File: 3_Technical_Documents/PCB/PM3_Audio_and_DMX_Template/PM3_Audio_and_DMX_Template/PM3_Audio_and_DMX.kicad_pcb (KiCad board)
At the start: 4 copper layers, 66 x 121.9 mm, 103 parts, among them J1 DMX-out, J2 LINE_IN, J3 LINE_OUT, P1 Conn_02x32_Odd_Even, P2 Conn_02x32_Odd_Even, SW1 SW_DPDT_x2, U1 6N136S, U11 OPA2134, U12 OPA2134, U13 TPA6110A2DGN, U2 CRE1S0505SC, U3 ST485E, U4 OPA322, U6 TLV61070ADBV, U7 LT3045xMSE, U8 LD3985M33R_SOT23, U9 CS4271

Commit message: new push
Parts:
- removed the R65 at (62.4, 132.7)
- removed the R8 at (44.0, 81.9)
- removed SW1: SW_DPDT_x2, Button_Switch_SMD:SW_DPDT_CK_JS202011JCQN
- removed U11: OPA2134, Package_SO:SOIC-8_3.9x4.9mm_P1.27mm
- added C10: 10u CER (rec. Murata GJ8), Capacitor_SMD:C_1210_3225Metric, F.Cu at (265.0, 71.9)
- added C26: 4.7u TANTAL, Capacitor_Tantalum_SMD:CP_EIA-3216-18_Kemet-A, F.Cu at (272.4, 77.6)
- added C27: 100n, Capacitor_SMD:C_0603_1608Metric, F.Cu at (269.9, 83.0)
- added C28: 4.7u CER, Capacitor_SMD:C_1210_3225Metric, F.Cu at (265.0, 83.9)
- added C29: 10u CER (rec. Murata GJ8), Capacitor_SMD:C_1210_3225Metric, F.Cu at (265.0, 88.2)
- added C3: 10u, Capacitor_SMD:C_1210_3225Metric, F.Cu at (250.4, 120.4)
- added C32: 100n, Capacitor_SMD:C_0603_1608Metric, F.Cu at (383.5, 85.0)
- added C33: 1u, Capacitor_SMD:C_0805_2012Metric, F.Cu at (386.0, 91.0)
- added C34: 47u, Capacitor_SMD:CP_Elec_6.3x7.7, F.Cu at (340.0, 87.5)
- added C35: 100n, Capacitor_SMD:C_0603_1608Metric, F.Cu at (245.6, 101.3)
- added C36: 1u, Capacitor_SMD:C_0805_2012Metric, F.Cu at (241.3, 97.0)
- added C37: 100n, Capacitor_SMD:C_0603_1608Metric, F.Cu at (245.6, 103.8)
- added C38: 1u, Capacitor_SMD:C_0805_2012Metric, F.Cu at (241.3, 100.0)
- added C39: 100n, Capacitor_SMD:C_0603_1608Metric, F.Cu at (249.6, 93.7)
- added C4: 10u, Capacitor_SMD:C_1210_3225Metric, F.Cu at (250.4, 124.7)
- added C40: 100n, Capacitor_SMD:C_0603_1608Metric, F.Cu at (249.6, 96.2)
- added C43: 1u, Capacitor_SMD:C_0805_2012Metric, F.Cu at (241.3, 106.0)
- added C44: 47u, Capacitor_SMD:CP_Elec_6.3x7.7, F.Cu at (233.9, 104.7)
- added C45: 10n COG/X7R, Capacitor_SMD:C_0603_1608Metric, F.Cu at (246.2, 61.0)
- added C46: 10n COG/X7R, Capacitor_SMD:C_0603_1608Metric, F.Cu at (246.2, 63.5)
- added C47: 10n COG/X7R, Capacitor_SMD:C_0603_1608Metric, F.Cu at (246.2, 66.0)
- added C49: 1u ELEC, Capacitor_SMD:CP_Elec_4x5.8, F.Cu at (340.0, 72.0)
- added C5: 100n, Capacitor_SMD:C_0603_1608Metric, F.Cu at (245.6, 119.5)
- added C50: 1u ELEC, Capacitor_SMD:CP_Elec_4x5.8, F.Cu at (232.5, 68.5)
- added C51: 1u ELEC, Capacitor_SMD:CP_Elec_4x5.8, F.Cu at (232.5, 74.4)
- added C53: 10u, Capacitor_SMD:CP_Elec_4x5.8, F.Cu at (232.5, 86.1)
- added C54: 10u, Capacitor_SMD:CP_Elec_4x5.8, F.Cu at (240.3, 62.7)
- added C55: 10u, Capacitor_SMD:CP_Elec_4x5.8, F.Cu at (240.3, 68.5)
- added C56: 10u, Capacitor_SMD:CP_Elec_4x5.8, F.Cu at (240.3, 74.4)
- added C57: 10n COG/X7R, Capacitor_SMD:C_0603_1608Metric, F.Cu at (246.2, 68.5)
- added C58: 10n COG/X7R, Capacitor_SMD:C_0603_1608Metric, F.Cu at (246.2, 71.0)
- added C59: 470p COG/X7R, Capacitor_SMD:C_0603_1608Metric, F.Cu at (246.2, 73.5)
- added C6: 100n, Capacitor_SMD:C_0603_1608Metric, F.Cu at (245.6, 122.0)
- added C60: 470p COG/X7R, Capacitor_SMD:C_0603_1608Metric, F.Cu at (246.2, 76.1)
- added C62: 470p COG/X7R, Capacitor_SMD:C_0603_1608Metric, F.Cu at (250.2, 63.5)
- added C63: 2n7 COG/X7R, Capacitor_SMD:C_0603_1608Metric, F.Cu at (250.2, 66.0)
- added C64: 2n7 COG/X7R, Capacitor_SMD:C_0603_1608Metric, F.Cu at (250.2, 68.5)
- added C65: 22u, Capacitor_SMD:CP_Elec_6.3x7.7, F.Cu at (362.0, 121.7)
- added C66: 2n2 COG, Capacitor_SMD:C_0603_1608Metric, F.Cu at (18.0, 220.7)
- added C67: 2n2 COG, Capacitor_SMD:C_0603_1608Metric, F.Cu at (16.0, 243.2)
- added C68: 6n8 COG, Capacitor_SMD:C_0603_1608Metric, F.Cu at (15.0, 222.8)
- added C69: 6n8 COG, Capacitor_SMD:C_0603_1608Metric, F.Cu at (4.50, 239.2)
- added C7: 4.7u TANTAL, Capacitor_Tantalum_SMD:CP_EIA-3216-18_Kemet-A, F.Cu at (272.4, 61.3)
- added C70: 2.2nF COG, Capacitor_SMD:C_0603_1608Metric, F.Cu at (382.7, 103.0)
- added C71: 22u, Capacitor_SMD:CP_Elec_6.3x7.7, F.Cu at (12.5, 216.8)
- added C72: 22u, Capacitor_SMD:CP_Elec_6.3x7.7, F.Cu at (7.00, 245.2)
- added C73: 1n5 COG, Capacitor_SMD:C_0603_1608Metric, F.Cu at (10.0, 222.8)
- added C74: 1n5 COG, Capacitor_SMD:C_0603_1608Metric, F.Cu at (9.72, 239.2)
- added C75: 10n COG/X7R, Capacitor_SMD:C_0603_1608Metric, F.Cu at (17.5, 233.8)
- added C76: 470p COG, Capacitor_SMD:C_0603_1608Metric, F.Cu at (18.0, 223.7)
- added C77: 470p COG, Capacitor_SMD:C_0603_1608Metric, F.Cu at (15.3, 237.8)
- added C78: 1u ELEC, Capacitor_SMD:CP_Elec_4x5.8, F.Cu at (7.00, 230.6)
- added C79: 22u, Capacitor_SMD:CP_Elec_6.3x7.7, F.Cu at (24.5, 232.6)
- added C8: 100n, Capacitor_SMD:C_0603_1608Metric, F.Cu at (269.9, 66.8)
- added C80: 22u, Capacitor_SMD:CP_Elec_6.3x7.7, F.Cu at (24.5, 241.6)
- added C9: 4.7u CER, Capacitor_SMD:C_1210_3225Metric, F.Cu at (265.0, 67.6)
- added J4: LINE_OUT, Connector_Audio:Jack_3.5mm_CUI_SJ-3523-SMT_Horizontal, F.Cu at (104.0, 55.0)
- added R2: 0R, Resistor_SMD:R_0603_1608Metric, F.Cu at (245.6, 124.5)
- added R27: 33k2, Resistor_SMD:R_0603_1608Metric, F.Cu at (269.9, 85.5)
- added R28: 200k, Resistor_SMD:R_0603_1608Metric, F.Cu at (269.9, 88.1)
- added R29: 10k, Resistor_SMD:R_0603_1608Metric, F.Cu at (345.0, 105.9)
- added R3: 10k, Resistor_SMD:R_0603_1608Metric, F.Cu at (245.6, 127.1)
- added R30: 10k, Resistor_SMD:R_0603_1608Metric, F.Cu at (349.5, 94.5)
- added R31: 10k, Resistor_SMD:R_0603_1608Metric, F.Cu at (350.0, 61.0)
- added R32: 10k, Resistor_SMD:R_0603_1608Metric, F.Cu at (363.0, 56.5)
- added R34: 10k, Resistor_SMD:R_0603_1608Metric, F.Cu at (254.2, 61.0)
- added R35: 10k, Resistor_SMD:R_0603_1608Metric, F.Cu at (254.2, 63.5)
- added R36: 10k, Resistor_SMD:R_0603_1608Metric, F.Cu at (254.2, 66.0)
- added R37: 634R, Resistor_SMD:R_0603_1608Metric, F.Cu at (254.2, 68.5)
- added R38: 634R, Resistor_SMD:R_0603_1608Metric, F.Cu at (254.2, 71.0)
- added R39: 634R, Resistor_SMD:R_0603_1608Metric, F.Cu at (254.2, 73.5)
- added R4: 10k, Resistor_SMD:R_0603_1608Metric, F.Cu at (245.6, 129.6)
- added R40: 634R, Resistor_SMD:R_0603_1608Metric, F.Cu at (254.2, 76.1)
- added R41: 91R, Resistor_SMD:R_0603_1608Metric, F.Cu at (258.2, 61.0)
- added R42: 91R, Resistor_SMD:R_0603_1608Metric, F.Cu at (258.2, 63.5)
- added R43: 91R, Resistor_SMD:R_0603_1608Metric, F.Cu at (258.2, 66.0)
- added R44: 91R, Resistor_SMD:R_0603_1608Metric, F.Cu at (258.2, 68.5)
- added R45: 4.99k, Resistor_SMD:R_0603_1608Metric, F.Cu at (342.5, 117.0)
- added R46: 4k42, Resistor_SMD:R_0603_1608Metric, F.Cu at (19.5, 220.7)
- added R47: 1k33, Resistor_SMD:R_0603_1608Metric, F.Cu at (15.0, 224.3)
- added R48: 4k42, Resistor_SMD:R_0603_1608Metric, F.Cu at (14.5, 243.2)
- added R49: 1k33, Resistor_SMD:R_0603_1608Metric, F.Cu at (4.50, 237.8)
- added R5: 10k, Resistor_SMD:R_0603_1608Metric, F.Cu at (245.6, 132.1)
- added R50: 1k5, Resistor_SMD:R_0603_1608Metric, F.Cu at (12.5, 223.8)
- added R51: 1k5, Resistor_SMD:R_0603_1608Metric, F.Cu at (7.00, 238.6)
- added R52: 2k32, Resistor_SMD:R_0603_1608Metric, F.Cu at (21.0, 223.7)
- added R53: 715R, Resistor_SMD:R_0603_1608Metric, F.Cu at (10.0, 224.3)
- added R54: 2k32, Resistor_SMD:R_0603_1608Metric, F.Cu at (14.5, 240.2)
- added R55: 715R, Resistor_SMD:R_0603_1608Metric, F.Cu at (9.72, 237.8)
- added R56: 4.99k, Resistor_SMD:R_0603_1608Metric, F.Cu at (19.5, 223.7)
- added R57: 4.99k, Resistor_SMD:R_0603_1608Metric, F.Cu at (16.0, 240.2)
- added R58: 560R, Resistor_SMD:R_0603_1608Metric, F.Cu at (31.0, 232.6)
- added R59: 560R, Resistor_SMD:R_0603_1608Metric, F.Cu at (31.0, 241.6)
- added R6: 33k2, Resistor_SMD:R_0603_1608Metric, F.Cu at (269.9, 69.3)
- added R60: 47k, Resistor_SMD:R_0603_1608Metric, F.Cu at (31.0, 234.1)
- added R61: 47k, Resistor_SMD:R_0603_1608Metric, F.Cu at (31.0, 243.1)
- added R7: 200k, Resistor_SMD:R_0603_1608Metric, F.Cu at (269.9, 71.8)
- added RV2: 50k stereo, Potentiometer_THT:Potentiometer_Bourns_PTV112-4_Dual_Vertical, F.Cu at (256.7, 97.9)
- added RV4: 50k stereo, Potentiometer_THT:Potentiometer_Bourns_PTV112-4_Dual_Vertical, F.Cu at (358.0, 99.3)
- added SW2: SW_DPDT_x2, Button_Switch_SMD:SW_DPDT_CK_JS202011JCQN, F.Cu at (248.9, 136.1)
- added SW3: SW_DPDT_x2, Button_Switch_SMD:SW_DPDT_CK_JS202011JCQN, F.Cu at (261.4, 137.9)
- added U1: ESP32-MINI-1, PCM_Espressif:ESP32-MINI-1, F.Cu at (120.1, 139.0)
- added U10: CS4271, Package_SO:TSSOP-28_4.4x9.7mm_P0.65mm, F.Cu at (247.9, 110.7)
- added U13: OPA2134, Package_SO:SOIC-8_3.9x4.9mm_P1.27mm, F.Cu at (248.4, 87.2)
- added U14: OPA2134, Package_SO:SOIC-8_3.9x4.9mm_P1.27mm, F.Cu at (13.5, 232.1)
- added U2: LT3045xMSE, Package_SO:MSOP-12-1EP_3x4.039mm_P0.65mm_EP1.651x2.845mm, F.Cu at (265.9, 62.7)
- C30: value 100n -> 40p
- C31: value 1u -> 40p; footprint Capacitor_SMD:C_0805_2012Metric -> Capacitor_SMD:C_0603_1608Metric
- C41: value 47u -> 100n; footprint Capacitor_SMD:CP_Elec_6.3x7.7 -> Capacitor_SMD:C_0603_1608Metric
- C42: value 1u ELEC -> 1u; footprint Capacitor_SMD:CP_Elec_4x5.8 -> Capacitor_SMD:C_0805_2012Metric
- C52: value 2.2nF COG -> 1u ELEC; footprint Capacitor_SMD:C_0603_1608Metric -> Capacitor_SMD:CP_Elec_4x5.8
- C61: value 22u -> 470p COG/X7R; footprint Capacitor_SMD:CP_Elec_6.3x7.7 -> Capacitor_SMD:C_0603_1608Metric
- J3: value LINE_OUT -> HEADPHONE_JACK
- RV1: value 50k -> 50k stereo; footprint Potentiometer_THT:Potentiometer_Bourns_PTV09A-1_Single_Vertical -> Potentiometer_THT:Potentiometer_Bourns_PTV112-4_Dual_Vertical
- RV3: value 50k stereo -> 50k; footprint Potentiometer_THT:Potentiometer_Bourns_PTV112-4_Dual_Vertical -> Potentiometer_THT:Potentiometer_Bourns_PTV09A-1_Single_Vertical
- U9: value CS4271 -> LT3045xMSE; footprint Package_SO:TSSOP-28_4.4x9.7mm_P0.65mm -> Package_SO:MSOP-12-1EP_3x4.039mm_P0.65mm_EP1.651x2.845mm
- moved RV3 326.9 mm to (352.4, 74.5), turned to 0 degrees
- moved C48 252.2 mm to (378.0, 63.9)
- moved U12 229.9 mm to (248.4, 80.7), turned to 0 degrees
- moved C41 225.8 mm to (249.6, 98.8)
- moved RV1 223.2 mm to (258.5, 123.7), turned to 0 degrees
- moved C42 221.5 mm to (241.3, 103.0), turned to 0 degrees
- moved U9 220.9 mm to (265.9, 79.0), turned to 0 degrees
- moved C61 219.1 mm to (250.2, 61.0)
- moved Y1 205.9 mm to (232.3, 111.4)
- moved C30 202.0 mm to (245.6, 93.7), turned to 0 degrees
- moved R33 196.1 mm to (250.2, 76.1), turned to 0 degrees
- moved C52 191.4 mm to (232.5, 80.2), turned to 0 degrees
- moved C31 183.4 mm to (245.6, 96.2), turned to 0 degrees
- moved J3 82.2 mm to (133.7, 142.4)
- moved J2 66.2 mm to (104.0, 43.5)
- renumbered C3 to C11, C4 to C12, C5 to C13, C6 to C14, C7 to C15, C8 to C16, C9 to C17, C10 to C18, C18 to C19, C19 to C20, C20 to C21, C21 to C22, C22 to C23, C23 to C24, C24 to C25, C63 to C81, C64 to C82, C65 to C83, C66 to C84, C67 to C85, C68 to C86, C69 to C87, C70 to C88, C71 to C89, R4 to R10, R5 to R11, R6 to R12, R7 to R13, R10 to R14, R11 to R15, R12 to R16, R13 to R17, R14 to R18, R15 to R19, R16 to R20, R25 to R21, R26 to R22, R27 to R23, R28 to R24, R29 to R25, R30 to R26, R70 to R62, R71 to R63, R72 to R64, R73 to R65, R74 to R66, R2 to R8, R3 to R9, TP14 to TP10, TP8 to TP6, TP9 to TP7, TP12 to TP8, TP13 to TP9, U13 to U15, U1 to U3, U2 to U4, U3 to U5, U4 to U6, U6 to U7, U7 to U8
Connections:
- C17 pad 2: +5VA -> VA
- C25 pad 1: +5VA -> VA
- C30 pad 1: unconnected-(C30-Pad1) -> GND
- C30 pad 2: unconnected-(C30-Pad2) -> XTI
- C31 pad 1: unconnected-(C31-Pad1) -> GND
- C31 pad 2: unconnected-(C31-Pad2) -> XTO
- C41 pad 1: unconnected-(C41-Pad1) -> GND
- C41 pad 2: unconnected-(C41-Pad2) -> Net-(U10-FILT+)
- C42 pad 1: unconnected-(C42-Pad1) -> VA
- C42 pad 2: unconnected-(C42-Pad2) -> GND
- C52 pad 1: unconnected-(C52-Pad1) -> VA
- C52 pad 2: unconnected-(C52-Pad2) -> GND
- C61 pad 1: unconnected-(C61-Pad1) -> Net-(C61-Pad1)
- C61 pad 2: unconnected-(C61-Pad2) -> Net-(U13A--)
- C86 pad 1: +5VA -> VA
- C89 pad 1: +5VA -> VA
- J2 pad R: unconnected-(J2-PadR) -> Jack_R
- J2 pad S: unconnected-(J2-PadS) -> GND
- J2 pad T: unconnected-(J2-PadT) -> Jack_L
- J3 pad R: unconnected-(J3-PadR) -> /PM3 Audio/Headphone Amplifier/out_r
- J3 pad S: unconnected-(J3-PadS) -> GND
- J3 pad T: unconnected-(J3-PadT) -> /PM3 Audio/Headphone Amplifier/out_l
- R15 pad 2: +5VA -> VA
- R16 pad 2: +5VA -> VA
- R25 pad 1: +5VA -> VA
- R33 pad 1: unconnected-(R33-Pad1) -> VCOM
- R33 pad 2: unconnected-(R33-Pad2) -> Net-(U12A-+)
- RV1 pad 1: unconnected-(RV1-Pad1) -> GND
- RV1 pad 2: unconnected-(RV1-Pad2) -> /PM3 Audio/Codec with analog line buffers/LINE_IN_R
- RV1 pad 3: unconnected-(RV1-Pad3) -> MIC_JACKR
- TP8 pad 1: +5VA -> VA
- U12 pad 1: unconnected-(U12-Pad1) -> Net-(C59-Pad1)
- U12 pad 2: unconnected-(U12A---Pad2) -> Net-(U12A--)
- U12 pad 3: unconnected-(U12A-+-Pad3) -> Net-(U12A-+)
- U12 pad 4: unconnected-(U12C-V--Pad4) -> GND
- U12 pad 5: unconnected-(U12B-+-Pad5) -> Net-(U12B-+)
- U12 pad 6: unconnected-(U12B---Pad6) -> Net-(U12B--)
- U12 pad 7: unconnected-(U12-Pad7) -> Net-(C60-Pad1)
- U12 pad 8: unconnected-(U12C-V+-Pad8) -> VA
- U15 pad 6: +5VA -> VA
- U6 pad 5: +5VA -> VA
- U8 pad 10: +5VA -> VA
- U8 pad 11: +5VA -> VA
- U8 pad 12: +5VA -> VA
- U9 pad 1: unconnected-(U9-XT0-Pad1) -> /PM3 Audio/Digital Power Supply/+5V
- U9 pad 10: unconnected-(U9-VL-Pad10) -> /PM3 Audio/Digital Power Supply/3V3
- U9 pad 11: unconnected-(U9-SCL/CCLK(M0)-Pad11) -> /PM3 Audio/Digital Power Supply/3V3
- U9 pad 12: unconnected-(U9-SDA/CDIN(M1)-Pad12) -> /PM3 Audio/Digital Power Supply/3V3
- U9 pad 13: unconnected-(U9-AD0/~{CS}(I2S/~{LJ})-Pad13) -> GND
- U9 pad 2: unconnected-(U9-XTI-Pad2) -> /PM3 Audio/Digital Power Supply/+5V
- U9 pad 3: unconnected-(U9-MCLK-Pad3) -> /PM3 Audio/Digital Power Supply/+5V
- U9 pad 4: unconnected-(U9-LRCK-Pad4) -> /PM3 Audio/Digital Power Supply/+5V
- U9 pad 5: unconnected-(U9-SCLK-Pad5) -> Net-(U9-PG)
- U9 pad 6: unconnected-(U9-SDOUT(M/~{S})-Pad6) -> GND
- U9 pad 7: unconnected-(U9-SDIN-Pad7) -> /PM3 Audio/Digital Power Supply/+5V
- U9 pad 8: unconnected-(U9-DGND-Pad8) -> Net-(U9-SET)
- U9 pad 9: unconnected-(U9-VD-Pad9) -> GND
- Y1 pad 1: unconnected-(Y1-Pad1) -> XTO
- Y1 pad 2: unconnected-(Y1-Pad2) -> XTI
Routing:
- net VA: track 0.00 -> 32.5 mm, vias 0 -> 2
- net +5VA: track 32.5 -> 0.00 mm, vias 2 -> 0
- added copper zone on B.Cu, net VA
- added copper zone on In2.Cu, net VA
- removed copper zone on B.Cu, net +5VA
- removed copper zone on In2.Cu, net +5VA

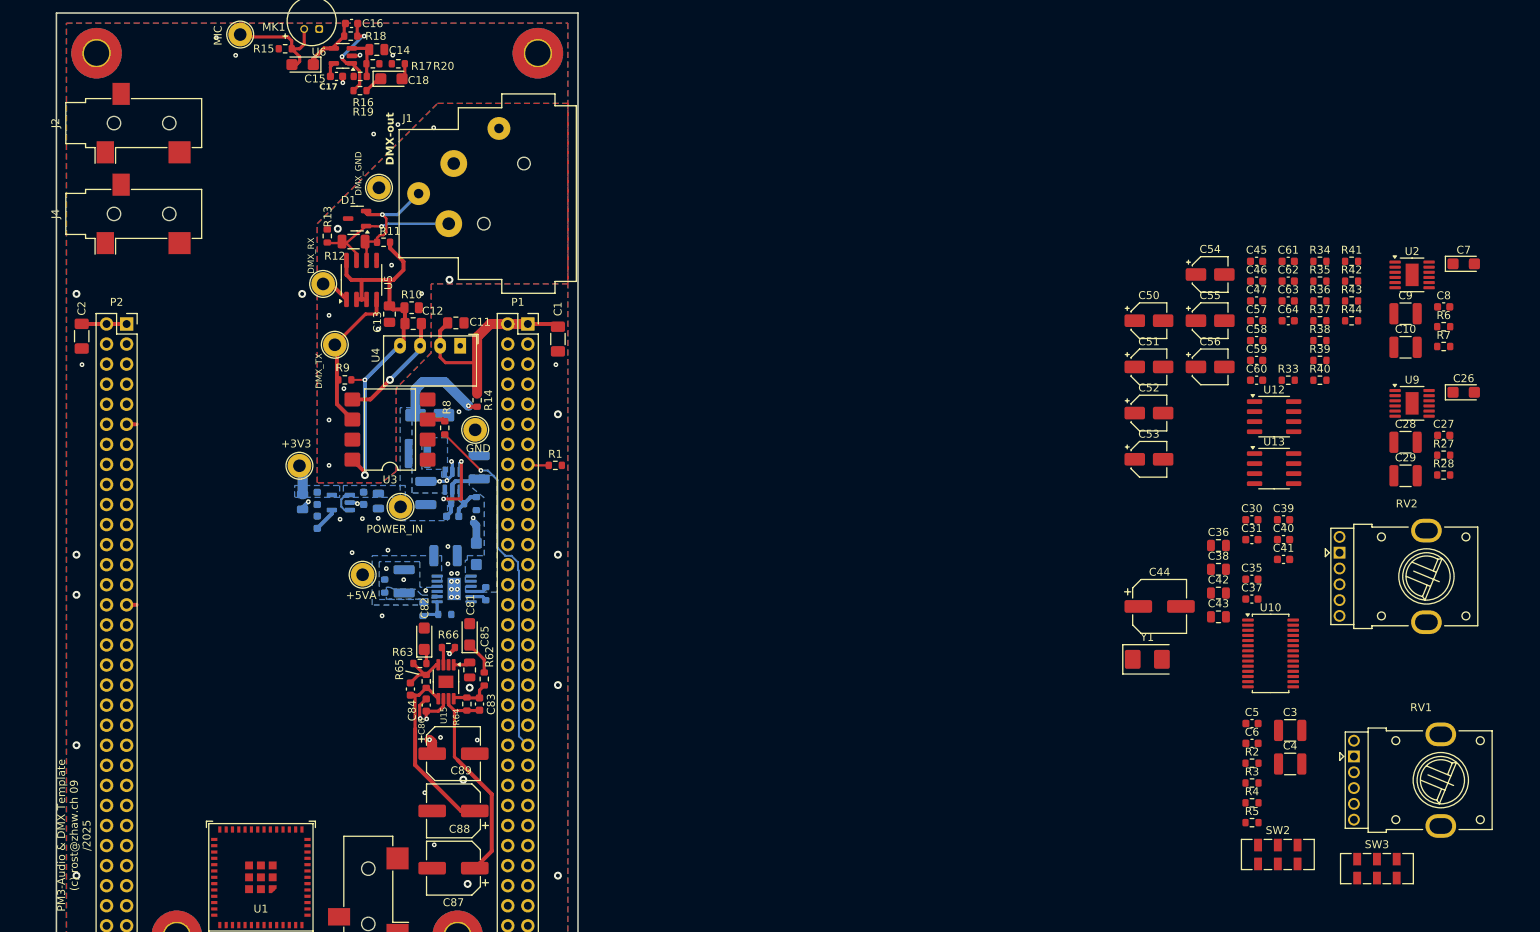
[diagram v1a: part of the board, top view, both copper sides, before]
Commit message: codec and layout
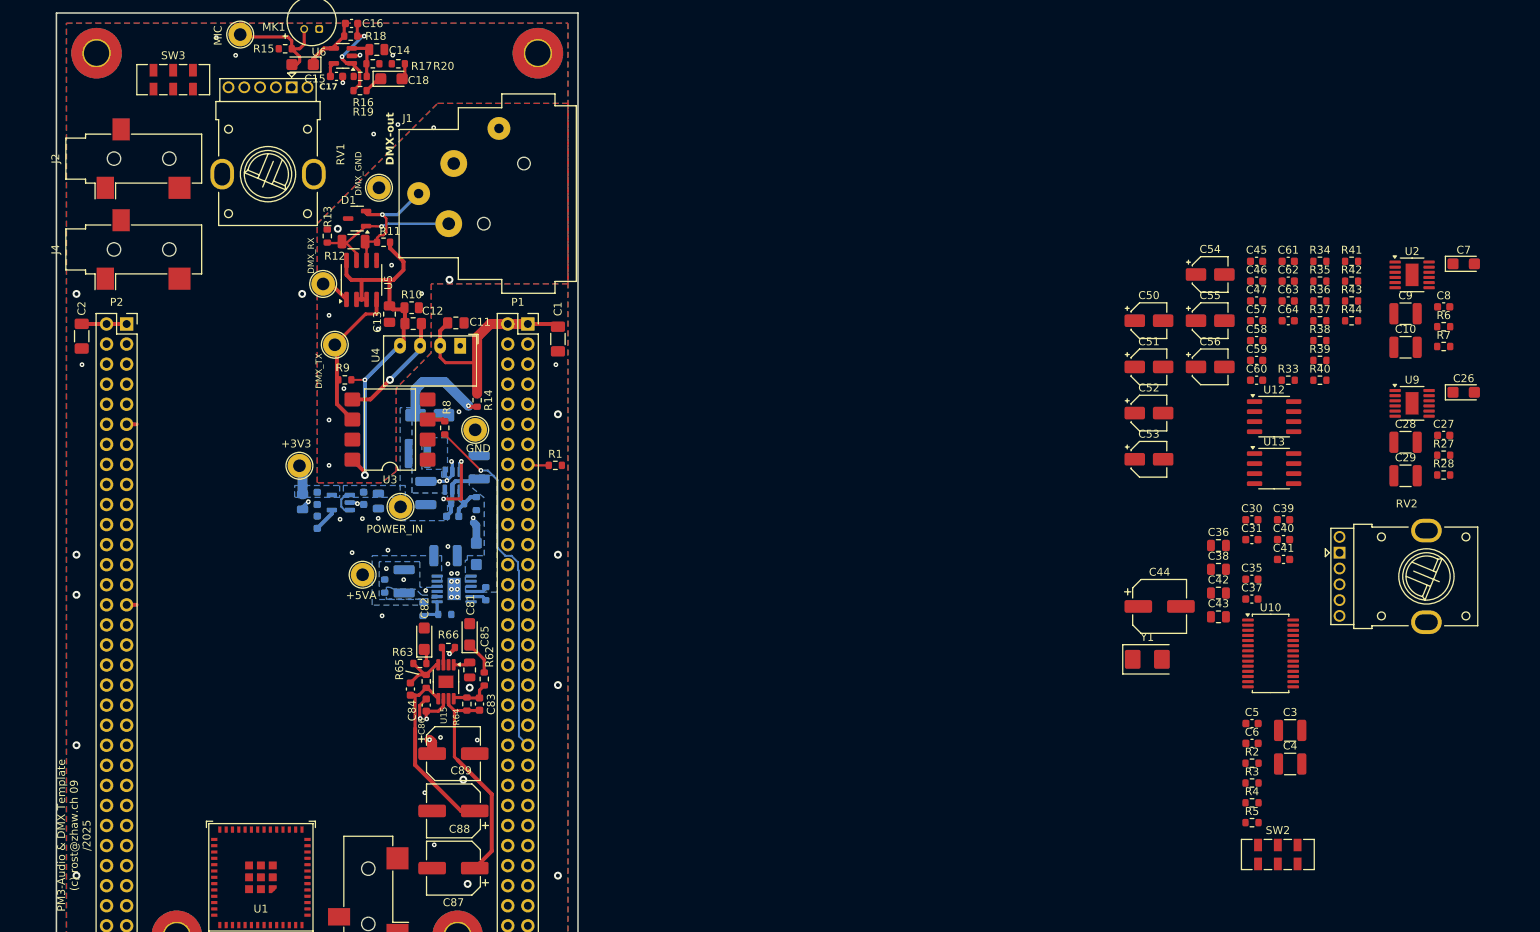
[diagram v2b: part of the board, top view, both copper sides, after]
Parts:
- moved SW3 182.2 mm to (109.0, 38.0)
- moved RV1 159.0 mm to (124.0, 39.0), turned to -90 degrees
- moved J2 4.50 mm to (104.0, 48.0)
- moved J4 4.50 mm to (104.0, 59.5)

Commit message: rework esp32, codec and layout
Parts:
- removed the C66 at (18.0, 220.7)
- removed the C67 at (16.0, 243.2)
- removed the C68 at (15.0, 222.8)
- removed the C69 at (4.50, 239.2)
- removed the C70 at (382.7, 103.0)
- removed the C71 at (12.5, 216.8)
- removed the C72 at (7.00, 245.2)
- removed the C73 at (10.0, 222.8)
- removed the C74 at (9.72, 239.2)
- removed C75: 10n COG/X7R, Capacitor_SMD:C_0603_1608Metric
- removed C76, C77: 470p COG, Capacitor_SMD:C_0603_1608Metric
- removed C78: 1u ELEC, Capacitor_SMD:CP_Elec_4x5.8
- removed C79, C80: 22u, Capacitor_SMD:CP_Elec_6.3x7.7
- removed the R59 at (31.0, 241.6)
- removed the R60 at (31.0, 234.1)
- removed the R61 at (31.0, 243.1)
- removed the R7 at (269.9, 71.8)
- removed RV3: 50k, Potentiometer_THT:Potentiometer_Bourns_PTV09A-1_Single_Vertical
- removed RV4: 50k stereo, Potentiometer_THT:Potentiometer_Bourns_PTV112-4_Dual_Vertical
- removed the SW2 at (248.9, 136.1)
- removed the U14 at (13.5, 232.1)
- added R1: 10k, Resistor_SMD:R_0603_1608Metric, F.Cu at (41.0, 133.0)
- added R26: 33k2, Resistor_SMD:R_0603_1608Metric, F.Cu at (231.4, 77.2)
- added SW2: SW_DPDT_x2, Button_Switch_SMD:SW_DPDT_CK_JS202011JCQN, F.Cu at (211.2, 114.7)
- added SW2: SW_DPDT_x2, Button_Switch_SMD:SW_DPDT_CK_JS202011JCQN, F.Cu at (33.8, 134.5)
- added U11: OPA2134, Package_SO:SOIC-8_3.9x4.9mm_P1.27mm, F.Cu at (168.5, -32.0)
- C34: value 47u -> 100n; footprint Capacitor_SMD:CP_Elec_6.3x7.7 -> Capacitor_SMD:C_0603_1608Metric
- C35, C39, C40: value 100n -> 1u; footprint Capacitor_SMD:C_0603_1608Metric -> Capacitor_SMD:C_0805_2012Metric
- C36, C38: value 1u -> 100n; footprint Capacitor_SMD:C_0805_2012Metric -> Capacitor_SMD:C_0603_1608Metric
- C41: value 100n -> 47u; footprint Capacitor_SMD:C_0603_1608Metric -> Capacitor_SMD:CP_Elec_6.3x7.7
- C42, C43: value 1u -> 10u; footprint Capacitor_SMD:C_0805_2012Metric -> Capacitor_SMD:CP_Elec_4x5.8
- C44: value 47u -> 470p COG/X7R; footprint Capacitor_SMD:CP_Elec_6.3x7.7 -> Capacitor_SMD:C_0603_1608Metric
- C45: value 10n COG/X7R -> 470p COG/X7R
- C46, C47: value 10n COG/X7R -> 2n7 COG/X7R
- C49: value 1u ELEC -> 10n COG/X7R; footprint Capacitor_SMD:CP_Elec_4x5.8 -> Capacitor_SMD:C_0603_1608Metric
- C52: value 1u ELEC -> 2n2 COG; footprint Capacitor_SMD:CP_Elec_4x5.8 -> Capacitor_SMD:C_0603_1608Metric
- C53: value 10u -> 2n2 COG; footprint Capacitor_SMD:CP_Elec_4x5.8 -> Capacitor_SMD:C_0603_1608Metric
- C54, C55: value 10u -> 6n8 COG; footprint Capacitor_SMD:CP_Elec_4x5.8 -> Capacitor_SMD:C_0603_1608Metric
- C56: value 10u -> 22u; footprint Capacitor_SMD:CP_Elec_4x5.8 -> Capacitor_SMD:CP_Elec_6.3x7.7
- C57: value 10n COG/X7R -> 22u; footprint Capacitor_SMD:C_0603_1608Metric -> Capacitor_SMD:CP_Elec_6.3x7.7
- C58: value 10n COG/X7R -> 1n5 COG
- C59: value 470p COG/X7R -> 1n5 COG
- C60: value 470p COG/X7R -> 10n COG/X7R
- C61, C62: value 470p COG/X7R -> 470p COG
- C63: value 2n7 COG/X7R -> 1u ELEC; footprint Capacitor_SMD:C_0603_1608Metric -> Capacitor_SMD:CP_Elec_4x5.8
- C64: value 2n7 COG/X7R -> 22u; footprint Capacitor_SMD:C_0603_1608Metric -> Capacitor_SMD:CP_Elec_6.3x7.7
- R2: value 0R -> 10k
- R27, R6: value 33k2 -> 200k
- R28: value 200k -> 10k
- R32: value 10k -> 47k
- R33, R34, R35, R36: value 10k -> 22R
- R37, R38: value 634R -> 10k
- R43: value 91R -> 4k42
- R44: value 91R -> 1k33
- R45: value 4.99k -> 4k42
- R46: value 4k42 -> 1k33
- R47: value 1k33 -> 1k5
- R48: value 4k42 -> 1k5
- R49: value 1k33 -> 2k32
- R5: value 10k -> 33k2
- R50: value 1k5 -> 715R
- R51: value 1k5 -> 2k32
- R52: value 2k32 -> 715R
- R53: value 715R -> 4.99k
- R54: value 2k32 -> 4.99k
- R55: value 715R -> 560R
- R56: value 4.99k -> 560R
- R57: value 4.99k -> 47k
- R58: value 560R -> 47k
- U1: value ESP32-MINI-1 -> ESP32-WROOM-32E; footprint PCM_Espressif:ESP32-MINI-1 -> RF_Module:ESP32-WROOM-32D; moved to B.Cu
- moved R55 291.5 mm to (100.9, -39.1), turned to 90 degrees
- moved R54 289.6 mm to (119.4, -29.6)
- moved R51 288.0 mm to (119.4, -26.6)
- moved C65 286.8 mm to (122.4, -36.1)
- moved R57 286.3 mm to (100.9, -33.1)
- moved R49 284.0 mm to (106.9, -27.1), turned to -90 degrees
- moved R56 283.9 mm to (126.9, -39.1), turned to 90 degrees
- moved R48 283.2 mm to (122.4, -18.6), turned to 180 degrees
- moved R58 282.5 mm to (126.9, -33.1), turned to 90 degrees
- moved R53 272.3 mm to (106.9, -30.1), turned to 90 degrees
- moved R45 264.0 mm to (120.9, -26.6), turned to 90 degrees
- moved R46 263.3 mm to (122.4, -21.6), turned to 0 degrees
- moved R50 262.0 mm to (104.0, -21.6), turned to 0 degrees
- moved R52 261.3 mm to (122.4, -17.1), turned to 180 degrees
- moved R47 260.2 mm to (104.0, -20.1), turned to 0 degrees
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- renumbered C81 to C66, C82 to C67, C83 to C68, C84 to C69, C85 to C70, C86 to C71, C87 to C72, C88 to C73, C89 to C74, R11 to R10, R12 to R11, R13 to R12, R14 to R13, R15 to R14, R16 to R15, R17 to R16, R18 to R17, R19 to R18, R20 to R19, R21 to R20, R22 to R21, R23 to R22, R24 to R23, R25 to R24, R26 to R25, R62 to R59, R63 to R60, R64 to R61, R65 to R62, R66 to R63, R8 to R7, R9 to R8, R10 to R9, U15 to U14
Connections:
- C2 pad 1: +3V0 -> VL
- C32 pad 1: unconnected-(C32-Pad1) -> VL
- C32 pad 2: unconnected-(C32-Pad2) -> GND
- C33 pad 1: unconnected-(C33-Pad1) -> VL
- C33 pad 2: unconnected-(C33-Pad2) -> GND
- C34 pad 1: unconnected-(C34-Pad1) -> VD
- C34 pad 2: unconnected-(C34-Pad2) -> GND
- C35 pad 1: VA -> VD
- C37 pad 1: VA -> VCOM
- C38 pad 1: VA -> GND
- C38 pad 2: GND -> Net-(U10-FILT+)
- C41 pad 1: GND -> Net-(U10-FILT+)
- C41 pad 2: Net-(U10-FILT+) -> GND
- C42 pad 1: VA -> Net-(U11A-+)
- C42 pad 2: GND -> /PM3 Audio/Codec with analog line buffers/LINE_IN_L
- C43 pad 1: VCOM -> Net-(U11B-+)
- C43 pad 2: GND -> /PM3 Audio/Codec with analog line buffers/LINE_IN_R
- C44 pad 1: Net-(U10-FILT+) -> Net-(C44-Pad1)
- C44 pad 2: GND -> Net-(U11A--)
- C45 pad 1: VA -> Net-(C45-Pad1)
- C45 pad 2: GND -> Net-(U11B--)
- C46 pad 1: VA -> /PM3 Audio/Codec with analog line buffers/Audio Input/AINA
- C46 pad 2: GND -> VCOM
- C47 pad 1: VA -> VCOM
- C47 pad 2: GND -> /PM3 Audio/Codec with analog line buffers/Audio Input/AINB
- C48 pad 1: unconnected-(C48-Pad1) -> VA
- C48 pad 2: unconnected-(C48-Pad2) -> GND
- C49 pad 1: unconnected-(C49-Pad1) -> VA
- C49 pad 2: unconnected-(C49-Pad2) -> GND
- C52 pad 1: VA -> GND
- C52 pad 2: GND -> Net-(C52-Pad2)
- C53 pad 1: Net-(U12A-+) -> GND
- C53 pad 2: /PM3 Audio/Codec with analog line buffers/LINE_IN_L -> Net-(C53-Pad2)
- C54 pad 1: Net-(U12B-+) -> GND
- C54 pad 2: /PM3 Audio/Codec with analog line buffers/LINE_IN_R -> Net-(C54-Pad2)
- C55 pad 1: Net-(U13A-+) -> GND
- C55 pad 2: /PM3 Audio/Codec with analog line buffers/LINE_IN_L -> Net-(C55-Pad2)
- C56 pad 1: Net-(U13B-+) -> Net-(C56-Pad1)
- C56 pad 2: /PM3 Audio/Codec with analog line buffers/LINE_IN_R -> GND
- C57 pad 1: GND -> Net-(C57-Pad1)
- C57 pad 2: VCOM -> GND
- C58 pad 2: VCOM -> Net-(U13A-+)
- C59 pad 1: Net-(C59-Pad1) -> GND
- C59 pad 2: Net-(U12A--) -> Net-(U13B-+)
- C60 pad 1: Net-(C60-Pad1) -> VA
- C60 pad 2: Net-(U12B--) -> GND
- C61 pad 1: Net-(C61-Pad1) -> Net-(U13A--)
- C61 pad 2: Net-(U13A--) -> Net-(C61-Pad2)
- C62 pad 1: Net-(C62-Pad1) -> Net-(U13B--)
- C62 pad 2: Net-(U13B--) -> Net-(C62-Pad2)
- C63 pad 1: /PM3 Audio/Codec with analog line buffers/Audio Input/AINA -> VA
- C63 pad 2: /PM3 Audio/Codec with analog line buffers/Audio Input/VQ2 -> GND
- C64 pad 1: /PM3 Audio/Codec with analog line buffers/Audio Input/AINB -> Net-(C61-Pad2)
- C64 pad 2: /PM3 Audio/Codec with analog line buffers/Audio Input/VQ3 -> Net-(C64-Pad2)
- C65 pad 1: unconnected-(C65-Pad1) -> Net-(C62-Pad2)
- C65 pad 2: unconnected-(C65-Pad2) -> Net-(C65-Pad2)
- P2 pad 1: +3V0 -> VL
- P2 pad 2: +3V0 -> VL
- P2 pad 49: unconnected-(P2-Pin_49-Pad49) -> _PB13
- P2 pad 50: unconnected-(P2-Pin_50-Pad50) -> _PB12
- P2 pad 51: unconnected-(P2-Pin_51-Pad51) -> _PB15
- P2 pad 52: unconnected-(P2-Pin_52-Pad52) -> _PB14
- R2 pad 1: /ESP32/Digital Power Supply/+5V -> EN
- R2 pad 2: +5V -> +3V3_ESP
- R27 pad 1: Net-(U9-SET) -> /PM3 Audio/Digital Power Supply/+5V
- R27 pad 2: GND -> Net-(U9-PG)
- R28 pad 1: /PM3 Audio/Digital Power Supply/+5V -> PA8
- R28 pad 2: Net-(U9-PG) -> VL
- R29 pad 1: unconnected-(R29-Pad1) -> GND
- R29 pad 2: unconnected-(R29-Pad2) -> PA8
- R3 pad 1: EN -> BOOT
- R3 pad 2: +3V3_ESP -> Net-(SW2A-B)
- R30 pad 1: unconnected-(R30-Pad1) -> PC9
- R30 pad 2: unconnected-(R30-Pad2) -> VL
- R31 pad 1: unconnected-(R31-Pad1) -> GND
- R31 pad 2: unconnected-(R31-Pad2) -> PC9
- R32 pad 1: unconnected-(R32-Pad1) -> PE6
- R32 pad 2: unconnected-(R32-Pad2) -> VL
- R33 pad 1: VCOM -> PE2
- R33 pad 2: Net-(U12A-+) -> Net-(U10-MCLK)
- R34 pad 1: Net-(U12B-+) -> Net-(U10-LRCK)
- R34 pad 2: VCOM -> PE4
- R35 pad 1: VCOM -> Net-(U10-SCLK)
- R35 pad 2: Net-(U13A-+) -> PE5
- R36 pad 1: Net-(U13B-+) -> Net-(U10-SDIN)
- R36 pad 2: VCOM -> PE3
- R37 pad 1: Net-(U12A--) -> VCOM
- R37 pad 2: /PM3 Audio/Codec with analog line buffers/Audio Input/AINA -> Net-(U11A-+)
- R38 pad 1: Net-(U12B--) -> Net-(U11B-+)
- R38 pad 2: /PM3 Audio/Codec with analog line buffers/Audio Input/VQ2 -> VCOM
- R39 pad 1: Net-(U13A--) -> Net-(U11A--)
- R39 pad 2: /PM3 Audio/Codec with analog line buffers/Audio Input/AINB -> /PM3 Audio/Codec with analog line buffers/Audio Input/AINA
- R4 pad 1: BOOT1 -> BOOT2
- R40 pad 1: Net-(U13B--) -> Net-(U11B--)
- R40 pad 2: /PM3 Audio/Codec with analog line buffers/Audio Input/VQ3 -> /PM3 Audio/Codec with analog line buffers/Audio Input/AINB
- R41 pad 1: Net-(C59-Pad1) -> Net-(C44-Pad1)
- R42 pad 1: Net-(C60-Pad1) -> Net-(C45-Pad1)
- R42 pad 2: /PM3 Audio/Codec with analog line buffers/Audio Input/VQ2 -> /PM3 Audio/Codec with analog line buffers/Audio Input/AINB
- R43 pad 1: Net-(C61-Pad1) -> /PM3 Audio/Codec with analog line buffers/Audio Output/AOUTA-
- R43 pad 2: /PM3 Audio/Codec with analog line buffers/Audio Input/AINB -> Net-(C52-Pad2)
- R44 pad 1: Net-(C62-Pad1) -> /PM3 Audio/Codec with analog line buffers/Audio Output/AOUTA+
- R44 pad 2: /PM3 Audio/Codec with analog line buffers/Audio Input/VQ3 -> Net-(C54-Pad2)
- R45 pad 1: unconnected-(R45-Pad1) -> /PM3 Audio/Codec with analog line buffers/Audio Output/AOUTB-
- R45 pad 2: unconnected-(R45-Pad2) -> Net-(C53-Pad2)
- R46 pad 1: /PM3 Audio/Codec with analog line buffers/Audio Output/AOUTA- -> /PM3 Audio/Codec with analog line buffers/Audio Output/AOUTB+
- R46 pad 2: Net-(C66-Pad2) -> Net-(C55-Pad2)
- R47 pad 1: /PM3 Audio/Codec with analog line buffers/Audio Output/AOUTA+ -> Net-(C54-Pad2)
- R47 pad 2: Net-(C68-Pad2) -> Net-(C56-Pad1)
- R48 pad 1: /PM3 Audio/Codec with analog line buffers/Audio Output/AOUTB- -> Net-(C55-Pad2)
- R48 pad 2: Net-(C67-Pad2) -> Net-(C57-Pad1)
- R49 pad 1: /PM3 Audio/Codec with analog line buffers/Audio Output/AOUTB+ -> Net-(C52-Pad2)
- R49 pad 2: Net-(C69-Pad2) -> Net-(U13A--)
- R5 pad 1: BOOT2 -> Net-(U2-SET)
- R5 pad 2: Net-(SW2B-B) (its old number) -> GND
- R50 pad 1: Net-(C68-Pad2) -> Net-(C54-Pad2)
- R50 pad 2: Net-(C71-Pad1) -> Net-(U13A-+)
- R51 pad 1: Net-(C69-Pad2) -> Net-(C53-Pad2)
- R51 pad 2: Net-(C72-Pad1) -> Net-(U13B--)
- R52 pad 1: Net-(C66-Pad2) -> Net-(C55-Pad2)
- R52 pad 2: Net-(U14A--) -> Net-(U13B-+)
- R53 pad 1: Net-(C68-Pad2) -> Net-(C52-Pad2)
- R53 pad 2: Net-(U14A-+) -> Net-(C61-Pad2)
- R54 pad 1: Net-(C67-Pad2) -> Net-(C53-Pad2)
- R54 pad 2: Net-(U14B--) -> Net-(C62-Pad2)
- R55 pad 1: Net-(C69-Pad2) -> Net-(C64-Pad2)
- R55 pad 2: Net-(U14B-+) -> /PM3 Audio/Codec with analog line buffers/LINE_OUT_L
- R56 pad 1: Net-(C66-Pad2) -> Net-(C65-Pad2)
- R56 pad 2: Net-(C76-Pad2) -> /PM3 Audio/Codec with analog line buffers/LINE_OUT_R
- R57 pad 1: Net-(C67-Pad2) -> GND
- R57 pad 2: Net-(C77-Pad2) -> /PM3 Audio/Codec with analog line buffers/LINE_OUT_L
- R58 pad 1: Net-(C79-Pad2) -> GND
- R58 pad 2: /PM3 Audio/Codec with analog line buffers/LINE_OUT_L -> /PM3 Audio/Codec with analog line buffers/LINE_OUT_R
- R6 pad 1: Net-(U2-SET) -> /ESP32/Digital Power Supply/+5V
- R6 pad 2: GND -> Net-(U2-PG)
- TP9 pad 1: +3.3V -> VD
- U1 pad 10: unconnected-(U1-VDET_2/GPIO35/ADC1_CH7-Pad10) -> LRCLK
- U1 pad 11: unconnected-(U1-32K_XP/GPIO32/ADC1_CH4-Pad11) -> BCLK
- U1 pad 13: unconnected-(U1-GPIO25/ADC2_CH8/DAC_1-Pad13) -> TMS
- U1 pad 14: unconnected-(U1-GPIO26/ADC2_CH9/DAC_2-Pad14) -> TDI
- U1 pad 15: unconnected-(U1-GPIO27/ADC2_CH7-Pad15) -> GND
- U1 pad 16: unconnected-(U1-MTMS/GPIO14/ADC2_CH6-Pad16) -> TCK
- U1 pad 2: GND -> +3V3_ESP
- U1 pad 20: BOOT2 -> unconnected-(U1-NC-Pad20)
- U1 pad 21: BOOT1 -> unconnected-(U1-NC-Pad21)
- U1 pad 23: unconnected-(U1-NC-Pad23) -> TDO
- U1 pad 25: unconnected-(U1-SD_DATA2/GPIO9-Pad25) -> MCLK
- U1 pad 27: GND -> unconnected-(U1-IO16-Pad27)
- U1 pad 28: unconnected-(U1-NC-Pad28) -> Net-(U1-IO17)
- U1 pad 3: +3V3_ESP -> EN
- U1 pad 34: unconnected-(U1-GPIO21-Pad34) -> Rx
- U1 pad 35: unconnected-(U1-U0RXD/GPIO3-Pad35) -> Tx
- U1 pad 36: unconnected-(U1-U0TXD/GPIO1-Pad36) -> DOUT
- U1 pad 37: unconnected-(U1-NC-Pad37) -> DIN
- U1 pad 8: EN -> unconnected-(U1-IO32-Pad8)
- U10 pad 10: VA -> VL
- U10 pad 13: unconnected-(U10-AD0/~{CS}(I2S/~{LJ})-Pad13) -> GND
- U10 pad 16: /PM3 Audio/Codec with analog line buffers/Audio Input/VQ2 -> VCOM
- U10 pad 19: /PM3 Audio/Codec with analog line buffers/Audio Input/VQ3 -> VCOM
- U10 pad 23: unconnected-(U10-~{AMUTEC}-Pad23) -> VL
- U10 pad 28: unconnected-(U10-~{BMUTEC}-Pad28) -> VL
- U10 pad 3: /PM3 Audio/MCLK -> Net-(U10-MCLK)
- U10 pad 4: PE4 -> Net-(U10-LRCK)
- U10 pad 5: PE5 -> Net-(U10-SCLK)
- U10 pad 7: PE3 -> Net-(U10-SDIN)
- U10 pad 9: VA -> VD
- U12 pad 1: Net-(C59-Pad1) -> VCOM
- U12 pad 2: Net-(U12A--) -> VCOM
- U12 pad 3: Net-(U12A-+) -> VCOM
- U12 pad 5: Net-(U12B-+) -> VCOM
- U12 pad 7: Net-(C60-Pad1) -> Net-(U12B--)
- U13 pad 1: Net-(C61-Pad1) -> Net-(C61-Pad2)
- U13 pad 7: Net-(C62-Pad1) -> Net-(C62-Pad2)
- U3 pad 2: +3V0 -> VL
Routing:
- net GND: track 18.3 -> 69.2 mm, vias 54 -> 79
- net VL: track 0.00 -> 37.3 mm, vias 0 -> 3
- net VCOM: track 0.00 -> 31.0 mm, vias 0 -> 2
- net /PM3 Audio/Codec with analog line buffers/LINE_OUT_L: track 0.00 -> 24.9 mm
- net Net-(U13B-+): track 0.00 -> 24.7 mm
- net /PM3 Audio/Codec with analog line buffers/LINE_OUT_R: track 0.00 -> 21.9 mm
- net /PM3 Audio/Codec with analog line buffers/Audio Output/AOUTB-: track 0.00 -> 21.5 mm
- net /PM3 Audio/Codec with analog line buffers/Audio Output/AOUTA-: track 0.00 -> 20.2 mm
- net /PM3 Audio/Codec with analog line buffers/Audio Output/AOUTB+: track 0.00 -> 19.3 mm
- net /ESP32/Digital Power Supply/+5V: track 0.00 -> 18.6 mm
- net Net-(U13A-+): track 0.00 -> 15.8 mm
- net VA: track 32.5 -> 48.2 mm
- net Net-(U13B--): track 0.00 -> 14.3 mm, vias 0 -> 2
- net Net-(C62-Pad2): track 0.00 -> 10.1 mm
- net Net-(U11A-+): track 0.00 -> 9.65 mm
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- added copper zone on B.Cu, net VD
- removed copper zone on B.Cu, net +3.3V
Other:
- board text added: "Analog Input"
- board text added: "Analog Output"
- board text added: "Codec"

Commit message: more layout
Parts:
- moved C30 216.3 mm to (207.2, -27.5)
- moved C31 216.3 mm to (210.2, -27.5)
- moved C37 216.3 mm to (213.2, -15.0)
- moved C38 216.3 mm to (216.8, -21.0)
- moved C40 216.3 mm to (213.2, -13.0)
- moved C41 216.3 mm to (223.4, -25.5)
- moved R28 216.3 mm to (204.3, -16.8)
- moved R29 216.3 mm to (205.8, -16.8)
- moved R30 216.3 mm to (204.3, -13.8)
- moved R31 216.3 mm to (205.8, -13.8)
- moved R32 216.3 mm to (205.2, -21.0)
- moved R33 216.3 mm to (205.2, -25.5)
- moved R34 216.3 mm to (205.2, -24.0)
- moved R35 216.3 mm to (205.2, -22.5)
- moved R36 216.3 mm to (205.2, -19.5)
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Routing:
- net GND: track 69.2 -> 92.5 mm, vias 79 -> 85
- net /PM3 Audio/Digital Power Supply/+5V: track 0.00 -> 18.0 mm
- net Net-(U9-SET): track 0.00 -> 5.58 mm
- net /PM3 Audio/Digital Power Supply/3V3: track 0.00 -> 3.61 mm
- net +3V3_ESP: track 1.30 -> 3.67 mm
- net Net-(U9-PG): track 0.00 -> 2.21 mm
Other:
- board text added: "ESP32 +3V3 Power"
- board text added: "PM3 +3V3 Power"
